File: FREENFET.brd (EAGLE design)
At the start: 17.8 x 17.8 mm, 12 parts, among them IC1 WS2811-SOP8, Q1 RJU003N03, Q2 NTD5867NLT4G

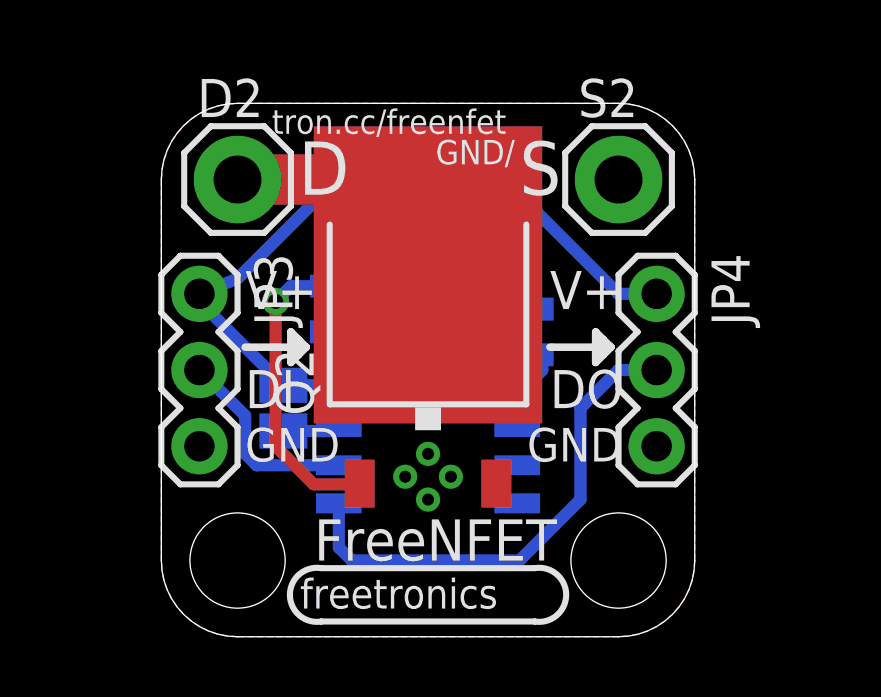
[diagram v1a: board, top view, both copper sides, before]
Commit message: Designator improvement
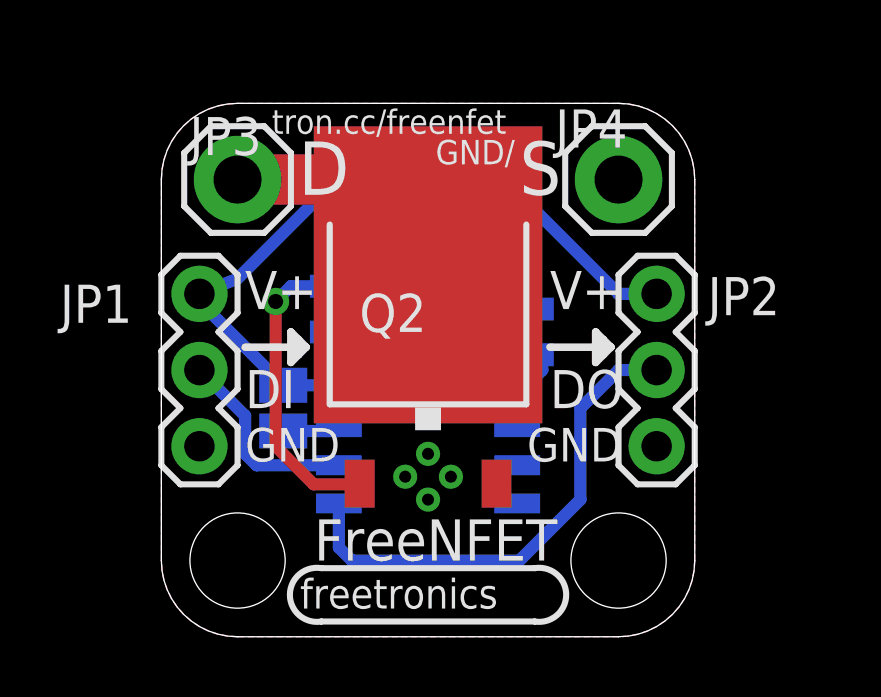
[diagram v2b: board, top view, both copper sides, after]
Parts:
- removed D2: DRAIN, freetronics-master-v1.1:1X01LARGE
- removed S2: SOURCE, freetronics-master-v1.1:1X01LARGE
- added JP1: IN, freetronics-jon:1X03
- added JP2: OUT, freetronics-jon:1X03
- JP3: value IN -> DRAIN; device freetronics-jon:1X03 -> freetronics-master-v1.1:1X01LARGE
- JP4: value OUT -> SOURCE; device freetronics-jon:1X03 -> freetronics-master-v1.1:1X01LARGE
- moved JP3 4.02 mm to (2.54, 15.2), turned to 0 degrees
- moved JP4 4.02 mm to (15.2, 15.2), turned to 0 degrees
- renumbered R5 to R3
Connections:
- net D: now also JP3.1; no longer D2.1
- net DIN: now also JP1.2; no longer JP3.2
- net DOUT: now also JP2.2; no longer JP4.2
- net GND: now also JP1.3, JP2.3, JP4.1; no longer JP3.3, JP4.3, S2.1
- net VCC: now also JP1.1, JP2.1; no longer JP3.1, JP4.1
